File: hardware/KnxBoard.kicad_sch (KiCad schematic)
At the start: 8 parts, among them J1 Conn_01x16, J2 Conn_01x16, J4 Conn_01x02_Male

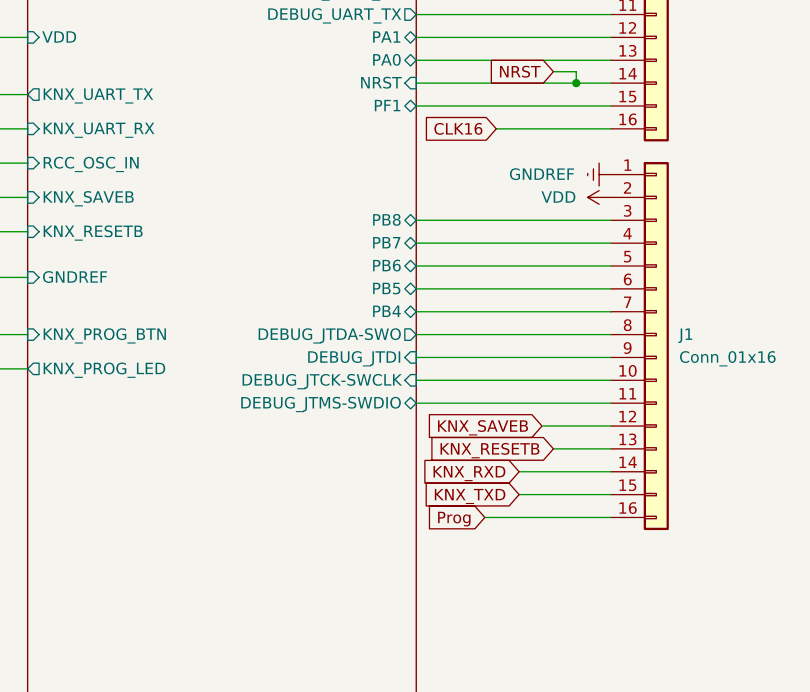
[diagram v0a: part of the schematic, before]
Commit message: Add 3D model and remove old parts
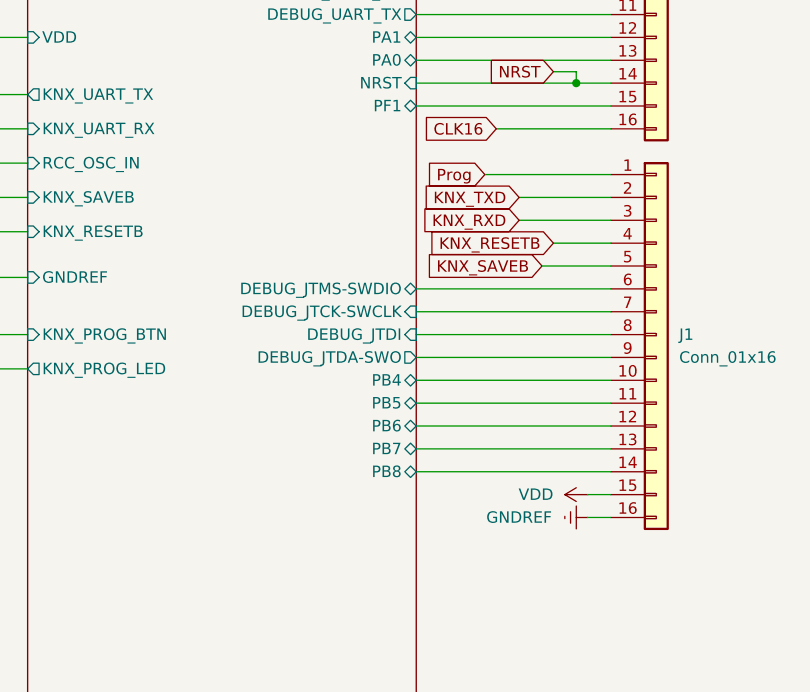
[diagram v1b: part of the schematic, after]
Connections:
- net GNDREF: now also J1.16 (Pin_16); no longer J1.1 (Pin_1)
- net KNX_RESETB: now also J1.4 (Pin_4); no longer J1.13 (Pin_13)
- net KNX_RXD: now also J1.3 (Pin_3); no longer J1.14 (Pin_14)
- net KNX_SAVEB: now also J1.5 (Pin_5); no longer J1.12 (Pin_12)
- net KNX_TXD: now also J1.2 (Pin_2); no longer J1.15 (Pin_15)
- net MCU/DEBUG_JTCK-SWCLK: now also J1.7 (Pin_7); no longer J1.10 (Pin_10)
- net MCU/DEBUG_JTDA-SWO: now also J1.9 (Pin_9); no longer J1.8 (Pin_8)
- net MCU/DEBUG_JTDI: now also J1.8 (Pin_8); no longer J1.9 (Pin_9)
- net MCU/DEBUG_JTMS-SWDIO: now also J1.6 (Pin_6); no longer J1.11 (Pin_11)
- net MCU/PB4: now also J1.10 (Pin_10); no longer J1.7 (Pin_7)
- net MCU/PB5: now also J1.11 (Pin_11); no longer J1.6 (Pin_6)
- net MCU/PB6: now also J1.12 (Pin_12); no longer J1.5 (Pin_5)
- net MCU/PB7: now also J1.13 (Pin_13); no longer J1.4 (Pin_4)
- net MCU/PB8: now also J1.14 (Pin_14); no longer J1.3 (Pin_3)
- net Prog: now also J1.1 (Pin_1); no longer J1.16 (Pin_16)
- net VDD: now also J1.15 (Pin_15); no longer J1.2 (Pin_2)

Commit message: Routage OK need check and mass and texts
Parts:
- removed J1, J2: Conn_01x16, Connector_PinHeader_2.54mm:PinHeader_1x16_P2.54mm_Vertical, symbol Connector_Generic:Conn_01x16
- removed J4: Conn_01x02_Male, KnxBoard:KNX_Connector, symbol Connector:Conn_01x02_Male
- added J1, J2: Conn_01x15, Connector_PinHeader_2.54mm:PinHeader_1x15_P2.54mm_Vertical, symbol Connector_Generic:Conn_01x15
- added TP1: KNX_RXD, TestPoint:TestPoint_Pad_D1.0mm, symbol Connector:TestPoint
- added TP2: KNX_TXD, TestPoint:TestPoint_Pad_D1.0mm, symbol Connector:TestPoint
- renumbered C18 to C30, JP3 to JP7, R21 to R30
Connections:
- net MCU/VDD is gone; now on net VDD: JP7.1 (A)
- net +12V: now also J1.1 (Pin_1)
- net CLK16: now also J2.15 (Pin_15)
- net GNDREF: now also J1.15 (Pin_15), J1.2 (Pin_2), J2.2 (Pin_2)
- net Led: now also J2.5 (Pin_5)
- net MCU/DEBUG_JTCK-SWCLK: now also J1.6 (Pin_6)
- net MCU/DEBUG_JTDA-SWO: now also J1.8 (Pin_8)
- net MCU/DEBUG_JTDI: now also J1.7 (Pin_7)
- net MCU/DEBUG_JTMS-SWDIO: now also J1.5 (Pin_5)
- net MCU/DEBUG_UART_RX: now also J2.10 (Pin_10)
- net MCU/DEBUG_UART_TX: now also J2.11 (Pin_11)
- net MCU/PA0: now also J2.13 (Pin_13)
- net MCU/PA1: now also J2.12 (Pin_12)
- net MCU/PA4: now also J2.9 (Pin_9)
- net MCU/PA5: now also J2.8 (Pin_8)
- net MCU/PA6: now also J2.7 (Pin_7)
- net MCU/PA7: now also J2.6 (Pin_6)
- net MCU/PB4: now also J1.9 (Pin_9)
- net MCU/PB5: now also J1.10 (Pin_10)
- net MCU/PB6: now also J1.11 (Pin_11)
- net MCU/PB7: now also J1.12 (Pin_12)
- net MCU/PB8: now also J1.13 (Pin_13)
- net MCU/PF1: now also J2.14 (Pin_14)
- net NRST: now also J1.4 (Pin_4)
- net Prog: now also J2.4 (Pin_4)
- net VDD: now also J1.14 (Pin_14), J2.3 (Pin_3)
- net KNXIFACE/+3.3V renamed +3V3
- new net KNXIFACE/KNX_RXD: TP1.1
- new net KNXIFACE/KNX_TXD: TP2.1
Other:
- sheet KNXIFACE ports: added none; removed +12V, +3.3V, GNDREF, KNX+, KNX-
- sheet MCU ports: added none; removed GNDREF, VDD

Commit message: Seed SeeedStudio N°1
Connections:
- net GNDREF: now also J1.3 (Pin_3), J2.1 (Pin_1)
- net MCU/DEBUG_JTDA-SWO renamed MCU/PB3
- net MCU/DEBUG_JTDI renamed MCU/PA15
- net NRST renamed MCU/NRST
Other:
- sheet MCU ports: added PA15, PB3; removed DEBUG_JTDA-SWO, DEBUG_JTDI
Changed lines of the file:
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@@
+    (stroke (width 0) (type default) (color 0 0 0 0))
+  )
+  (wire (pts (xy 196.85 100.33) (xy 218.44 100.33))
     (stroke (width 0) (type default) (color 0 0 0 0))
   )
@@
     (effects (font (size 1.27 1.27)) (justify right))
     (property "Références Inter-Feuilles" "${INTERSHEET_REFS}" (id 0) (at -54.61 24.13 0)
-      (effects (font (size 1.27 1.27)) hide)
-    )
-  )
-  (global_label "NRST" (shape input) (at 196.85 93.98 0) (fields_autoplaced)
-    (effects (font (size 1.27 1.27)) (justify left))
-    (property "Références Inter-Feuilles" "${INTERSHEET_REFS}" (id 0) (at 469.9 137.16 0)
       (effects (font (size 1.27 1.27)) hide)
     )
@@
     (effects (font (size 1.27 1.27)) (justify right))
     (property "Références Inter-Feuilles" "${INTERSHEET_REFS}" (id 0) (at -153.67 78.74 0)
-      (effects (font (size 1.27 1.27)) hide)
-    )
-  )
-  (global_label "NRST" (shape input) (at 218.44 100.33 180) (fields_autoplaced)
-    (effects (font (size 1.27 1.27)) (justify right))
-    (property "Références Inter-Feuilles" "${INTERSHEET_REFS}" (id 0) (at -54.61 57.15 0)
       (effects (font (size 1.27 1.27)) hide)
     )
@@
     (pin "1")
   )
+  (symbol (lib_id "power:GNDREF") (at 218.44 49.53 270) (unit 1)
+    (in_bom yes) (on_board yes)
+    (property "Reference" "#PWR0146" (id 0) (at 212.09 49.53 0)
+      (effects (font (size 1.27 1.27)) hide)
+    )
+    (property "Value" "GNDREF" (id 1) (at 210.82 49.53 90))
+    (property "Footprint" "" (id 2) (at 218.44 49.53 0)
+      (effects (font (size 1.27 1.27)) hide)
+    )
+    (property "Datasheet" "" (id 3) (at 218.44 49.53 0)
+      (effects (font (size 1.27 1.27)) hide)
+    )
+    (pin "1")
+  )
   (symbol (lib_id "Jumper:SolderJumper_2_Open") (at 107.95 74.93 180) (unit 1)
     (in_bom yes) (on_board yes) (fields_autoplaced)
@@
     (pin "2")
   )
+  (symbol (lib_id "power:GNDREF") (at 218.44 97.79 270) (unit 1)
+    (in_bom yes) (on_board yes)
+    (property "Reference" "#PWR0147" (id 0) (at 212.09 97.79 0)
+      (effects (font (size 1.27 1.27)) hide)
+    )
+    (property "Value" "GNDREF" (id 1) (at 210.82 97.79 90))
+    (property "Footprint" "" (id 2) (at 218.44 97.79 0)
+      (effects (font (size 1.27 1.27)) hide)
+    )
+    (property "Datasheet" "" (id 3) (at 218.44 97.79 0)
+      (effects (font (size 1.27 1.27)) hide)
+    )
+    (pin "1")
+  )
   (symbol (lib_id "power:VDD") (at 149.86 74.93 0) (unit 1)
     (in_bom yes) (on_board yes)
@@
       (effects (font (size 1.27 1.27)) (justify left top))
     )
-    (pin "DEBUG_JTDI" input (at 196.85 107.95 0)
-      (effects (font (size 1.27 1.27)) (justify right))
-    )
     (pin "KNX_UART_TX" output (at 153.67 81.28 180)
       (effects (font (size 1.27 1.27)) (justify left))
@@
       (effects (font (size 1.27 1.27)) (justify right))
     )
-    (pin "DEBUG_JTDA-SWO" output (at 196.85 110.49 0)
-      (effects (font (size 1.27 1.27)) (justify right))
-    )
     (pin "RCC_OSC_IN" input (at 153.67 88.9 180)
       (effects (font (size 1.27 1.27)) (justify left))
@@
       (effects (font (size 1.27 1.27)) (justify left))
     )
-    (pin "NRST" input (at 196.85 93.98 0)
+    (pin "NRST" input (at 196.85 100.33 0)
       (effects (font (size 1.27 1.27)) (justify right))
     )
@@
     )
     (pin "PB4" bidirectional (at 196.85 113.03 0)
+      (effects (font (size 1.27 1.27)) (justify right))
+    )
+    (pin "PB3" bidirectional (at 196.85 110.49 0)
+      (effects (font (size 1.27 1.27)) (justify right))
+    )
+    (pin "PA15" bidirectional (at 196.85 107.95 0)
       (effects (font (size 1.27 1.27)) (justify right))
     )
@@
       (reference "#PWR0128") (unit 1) (value "GNDREF") (footprint "")
     )
-    (path "/60177bd8-6562-4452-843e-ff6a093b4415/596176df-6ec0-47cb-ba5d-eb880201ae94"
-      (reference "#PWR0129") (unit 1) (value "+3V3") (footprint "")
-    )
     (path "/d8441614-dec4-4bc1-b184-c502a3d79ed5/94eb79da-aa58-4752-8a69-ac0221cde80c"
       (reference "#PWR0130") (unit 1) (value "GNDREF") (footprint "")
@@
       (reference "#PWR0145") (unit 1) (value "GNDREF") (footprint "")
     )
+    (path "/9e8a9a69-730d-403b-9b12-29bfaaec4f9e"
+      (reference "#PWR0146") (unit 1) (value "GNDREF") (footprint "")
+    )
+    (path "/e11202c5-06de-4d6a-ac14-d8fb54d9902e"
+      (reference "#PWR0147") (unit 1) (value "GNDREF") (footprint "")
+    )
     (path "/d8441614-dec4-4bc1-b184-c502a3d79ed5/c65a92da-c4a5-4c10-b6a8-a8567a5c1b51"
